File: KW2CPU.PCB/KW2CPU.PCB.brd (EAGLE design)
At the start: 50 x 30 mm, 49 parts, among them IC1 AT45DB161D8S1

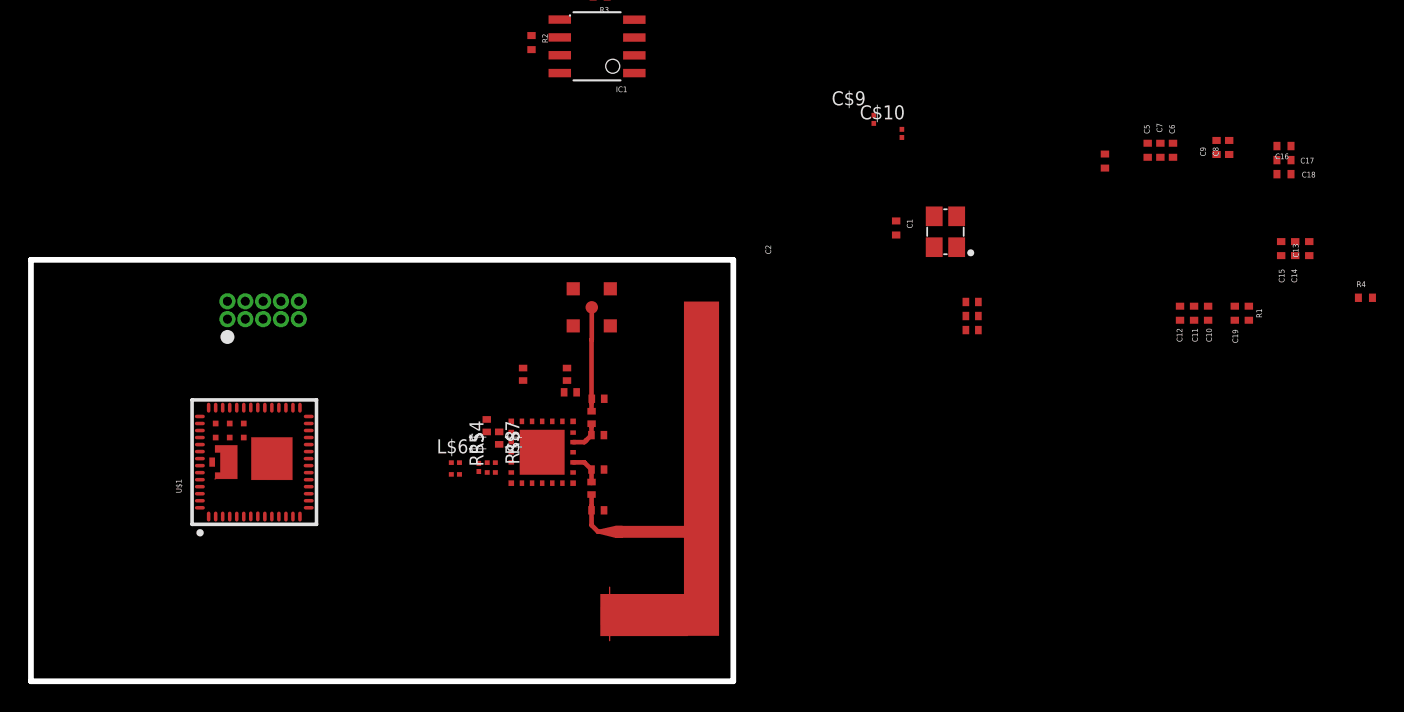
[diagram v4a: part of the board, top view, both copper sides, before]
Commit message: Brain component placement
Almost finished KW2CPU component placement. Needs JTAG and memory
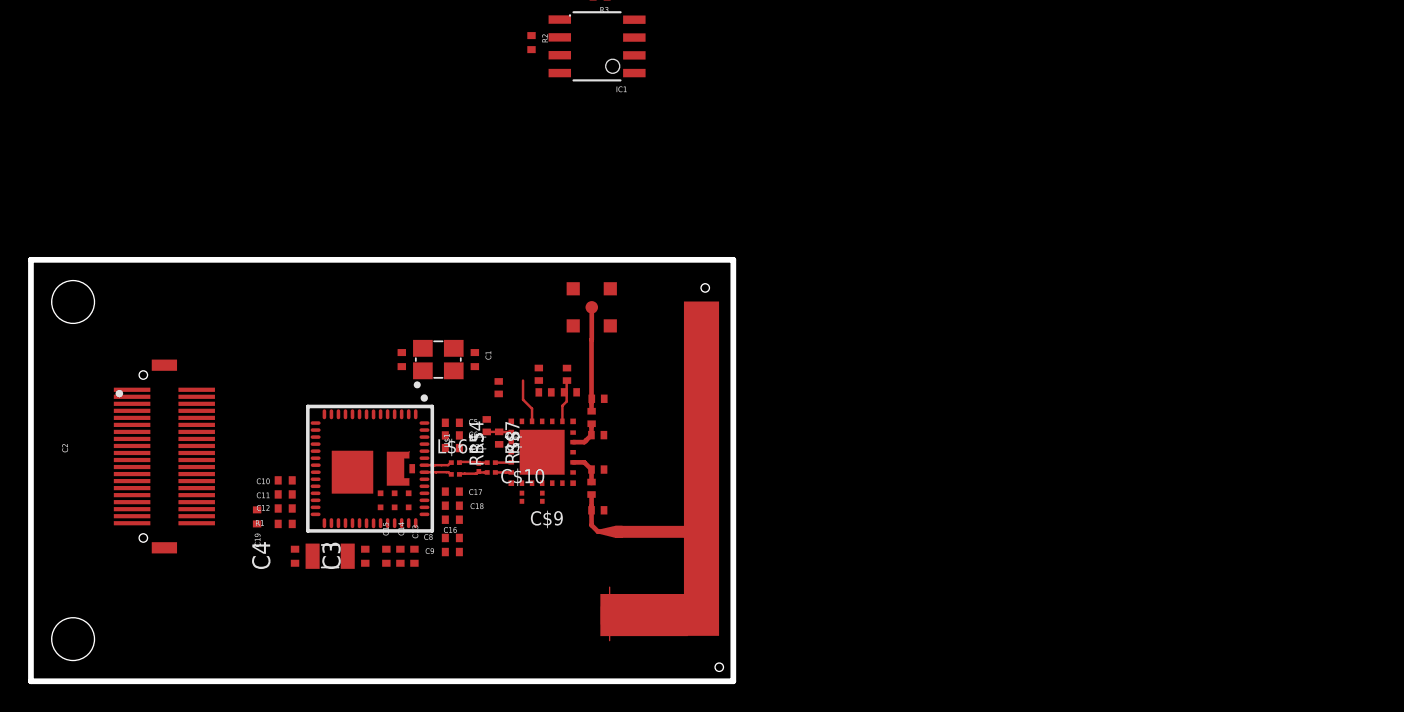
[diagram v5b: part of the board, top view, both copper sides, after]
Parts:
- removed JP1: (no value), KW2:2X5HDR
- removed R$12: (no value), GW-devices:RFMD0402
- removed R4: 10k, GW-devices:RF-R0402
- added C3, C4: 12pF, GW-devices:C0402
- added U$6: DF12_M, KW2:DF12_M
- added U$7: 32KHZ, KW2:32KHZSMD
- moved C19 71.1 mm to (-26.9, -9.30)
- moved R1 70.2 mm to (-24.9, -9.80), turned to 0 degrees
- moved C13 67.4 mm to (-15.7, -12.1), turned to 270 degrees
- moved C14 67.4 mm to (-16.7, -12.1), turned to 270 degrees
- moved C15 67.4 mm to (-17.7, -12.1), turned to 270 degrees
- moved C10 66.8 mm to (-24.9, -6.70), turned to 180 degrees
- moved C11 66.0 mm to (-24.9, -7.70), turned to 180 degrees
- moved C12 65.2 mm to (-24.9, -8.70), turned to 180 degrees
- moved C16 64.9 mm to (-13.0, -9.50)
- moved C17 63.7 mm to (-13.0, -7.50)
- moved C18 63.7 mm to (-13.0, -8.50)
- moved C8 61.9 mm to (-13.0, -10.8), turned to 0 degrees
- moved C9 61.6 mm to (-13.0, -11.8), turned to 0 degrees
- moved C6 55.2 mm to (-13.0, -3.50), turned to 0 degrees
- moved C7 54.7 mm to (-13.0, -4.40), turned to 0 degrees
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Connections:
- removed net N$29: R$12.P$1, U$3.P$23
- new net N$28: C3.1, U$1.P$31, U$7.P$1
- new net N$32: C4.1, U$1.P$30, U$7.P$2
- new net N$33: U$1.P$9, U$6.P$3
- new net N$34: U$1.P$8, U$6.P$1
- new net N$35: U$1.P$10, U$6.P$5
- new net N$36: U$1.P$11, U$6.P$7
- new net N$37: U$1.P$12, U$6.P$9
- new net N$38: U$1.P$13, U$6.P$11
- new net N$39: U$1.P$14, U$6.P$13
- new net N$40: U$1.P$15, U$6.P$15
- new net N$41: U$1.P$16, U$6.P$17
- new net N$42: U$1.P$17, U$6.P$19
- new net N$43: U$1.P$18, U$6.P$21
- new net N$44: U$1.P$19, U$6.P$23
- new net N$45: U$1.P$21, U$6.P$25
- new net N$46: U$1.P$22, U$6.P$27
- new net N$47: U$1.P$23, U$6.P$29
- new net N$48: U$1.P$24, U$6.P$31
- new net N$49: U$1.P$39, U$6.P$14
- new net N$50: U$1.P$40, U$6.P$16
- net +3V3: no longer JP1.P$1, R4.2
- net GND: now also C3.2, C4.2, U$3.P$23; no longer JP1.P$3, JP1.P$5, R$12.P$2
- net N$10: now also U$1.P$33, U$6.P$4; no longer JP1.P$2, U$1.P$36
- net N$11: now also U$1.P$34, U$6.P$6; no longer JP1.P$4, U$1.P$33
- net N$12: now also U$6.P$8; no longer JP1.P$6
- net N$13: now also U$1.P$36, U$6.P$10; no longer JP1.P$8, U$1.P$34
- net N$14: now also U$6.P$2; no longer JP1.P$10
- net N$15: now also U$1.P$37, U$6.P$12; no longer JP1.P$9, R4.1
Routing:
- net N$27: track 0.00 -> 3.24 mm
- net GND: track 0.00 -> 3.17 mm
- net N$5: track 0.00 -> 2.09 mm
- net N$4: track 0.00 -> 2.06 mm
- net N$3: track 0.00 -> 1.99 mm
- net N$2: track 0.00 -> 1.98 mm
- net N$30: track 0.00 -> 1.75 mm
- net N$19: track 0.00 -> 1.14 mm
- net N$20: track 0.00 -> 1.13 mm
